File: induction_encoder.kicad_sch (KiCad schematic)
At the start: 69 parts, among them J402 Conn_01x06, U1 MT9105ET, U10 IPS2200, U11 ADS1115IDGS, U12 ADS1115IDGS, U2 MT9105ET, U4 MT9105ET, U5 MT9105ET, U7 ADS1115IDGS, U8 MT9105ET

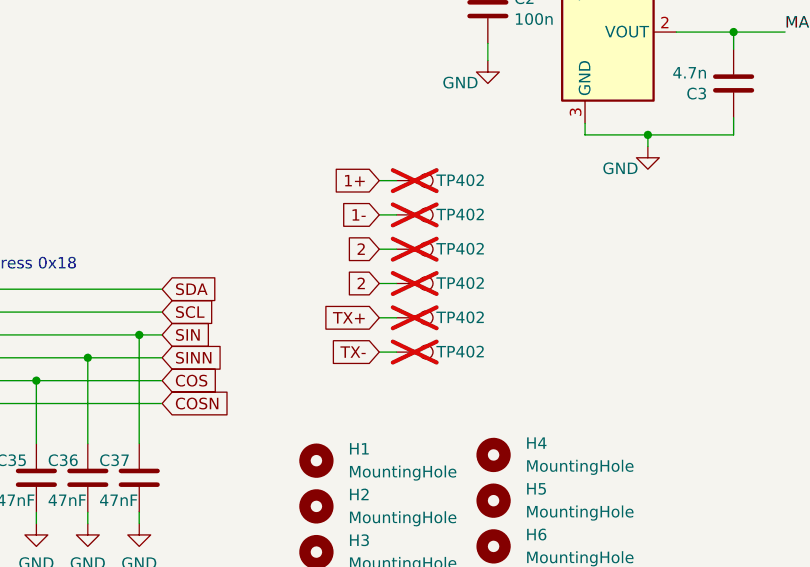
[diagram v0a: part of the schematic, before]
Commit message: Updated to larger encoder size.
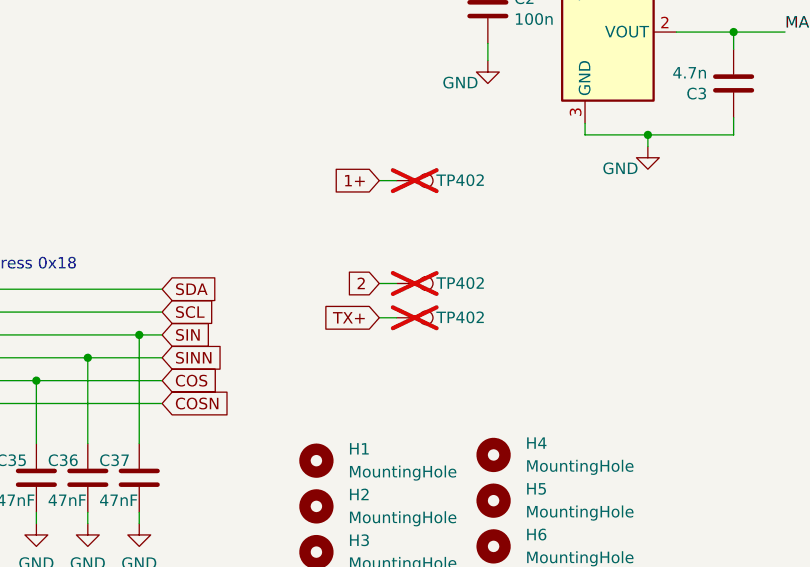
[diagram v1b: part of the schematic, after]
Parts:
- removed TP402 (x3): TestPoint, TestPoint:TestPoint_Pad_D2.0mm, symbol Connector:TestPoint
